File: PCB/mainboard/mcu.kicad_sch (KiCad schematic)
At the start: 10 parts

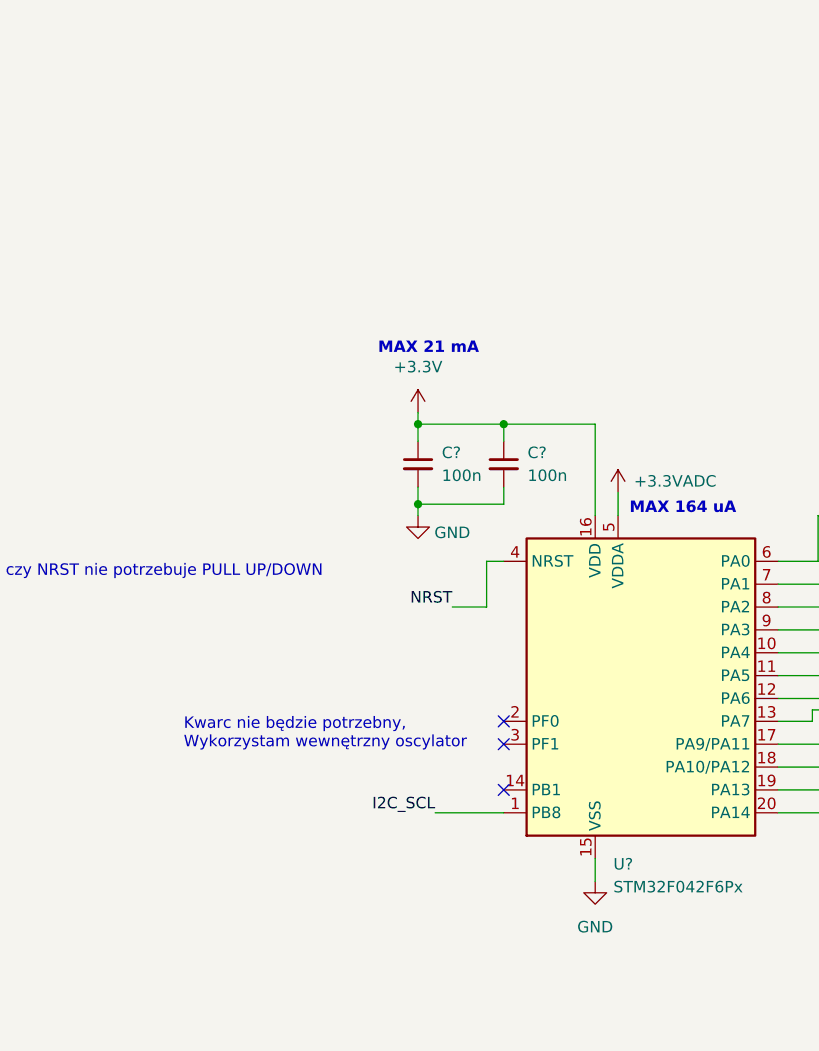
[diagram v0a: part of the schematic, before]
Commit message: Added power up/down push button
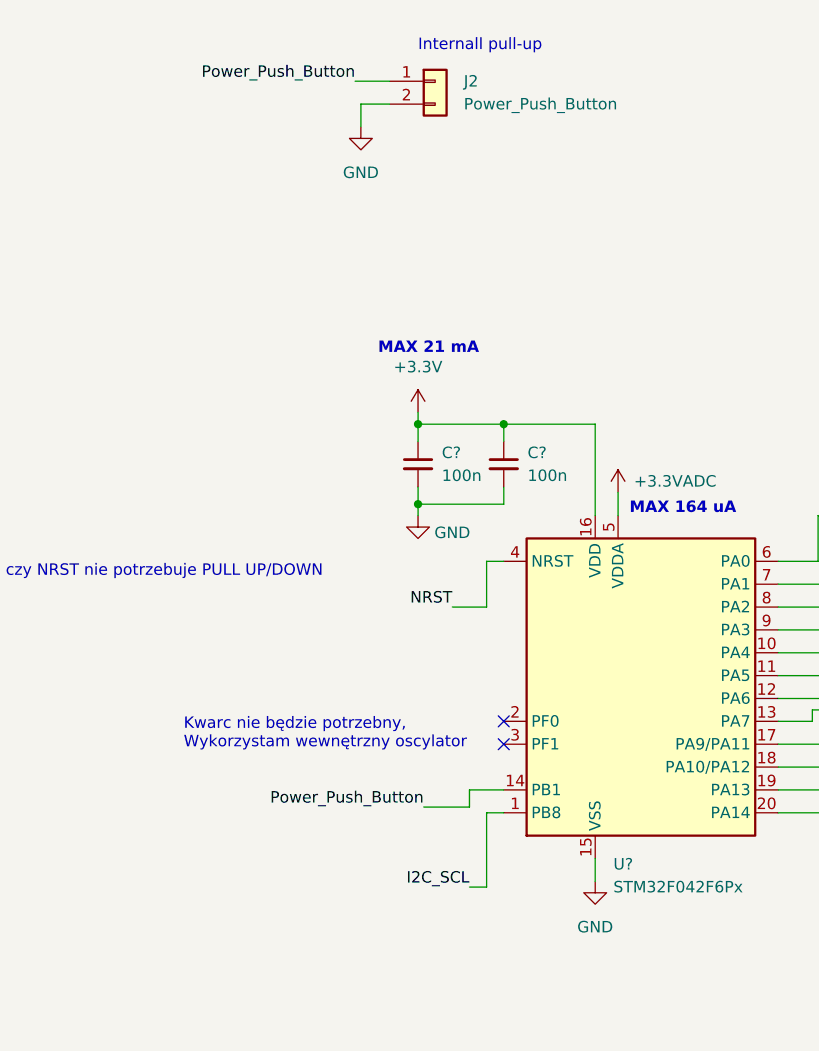
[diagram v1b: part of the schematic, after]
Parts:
- added J2: Power_Push_Button, symbol Connector_Generic:Conn_01x02
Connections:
- net GND: now also J2.2 (Pin_2)
- net Power_Push_Button: now reaches U?.14 (PB1)
- net Power_Push_Button: now also J2.1 (Pin_1)
- no-connect marks 3 -> 2
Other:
- note added: "Internall pull-up"
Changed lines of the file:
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@@
   (junction (at 219.71 131.445) (diameter 0) (color 0 0 0 0)
   )
-  (no_connect (at 120.65 107.95))
   (no_connect (at 120.65 102.87))
   (no_connect (at 120.65 100.33))
@@
     (stroke (width 0) (type default))
   )
-  (wire (pts (xy 113.03 110.49) (xy 120.65 110.49))
+  (wire (pts (xy 116.84 118.745) (xy 118.745 118.745))
     (stroke (width 0) (type default))
   )
@@
     (stroke (width 0) (type default))
   )
+  (wire (pts (xy 104.775 31.75) (xy 107.95 31.75))
+    (stroke (width 0) (type default))
+  )
   (wire (pts (xy 151.13 92.71) (xy 156.21 92.71))
     (stroke (width 0) (type default))
@@
     (stroke (width 0) (type default))
   )
+  (wire (pts (xy 104.775 34.29) (xy 104.775 31.75))
+    (stroke (width 0) (type default))
+  )
   (wire (pts (xy 233.68 58.42) (xy 238.76 58.42))
     (stroke (width 0) (type default))
@@
     (stroke (width 0) (type default))
   )
+  (wire (pts (xy 118.745 118.745) (xy 118.745 110.49))
+    (stroke (width 0) (type default))
+  )
+  (wire (pts (xy 116.84 107.95) (xy 120.65 107.95))
+    (stroke (width 0) (type default))
+  )
   (wire (pts (xy 172.72 34.925) (xy 172.72 34.29))
     (stroke (width 0) (type default))
@@
     (stroke (width 0) (type default))
   )
+  (wire (pts (xy 116.84 109.855) (xy 116.84 107.95))
+    (stroke (width 0) (type default))
+  )
   (wire (pts (xy 233.045 38.1) (xy 238.125 38.1))
     (stroke (width 0) (type default))
@@
     (stroke (width 0) (type default))
   )
+  (wire (pts (xy 104.14 29.21) (xy 107.95 29.21))
+    (stroke (width 0) (type default))
+  )
   (wire (pts (xy 114.935 87.63) (xy 118.745 87.63))
     (stroke (width 0) (type default))
@@
     (stroke (width 0) (type default))
   )
+  (wire (pts (xy 118.745 110.49) (xy 120.65 110.49))
+    (stroke (width 0) (type default))
+  )
   (wire (pts (xy 130.81 77.47) (xy 130.81 67.31))
     (stroke (width 0) (type default))
@@
   )
   (wire (pts (xy 154.94 99.06) (xy 154.94 100.33))
+    (stroke (width 0) (type default))
+  )
+  (wire (pts (xy 111.76 109.855) (xy 116.84 109.855))
     (stroke (width 0) (type default))
   )
@@
     (effects (font (size 1.27 1.27)) (justify left bottom))
   )
+  (text "Internall pull-up" (at 111.125 26.035 0)
+    (effects (font (size 1.27 1.27)) (justify left bottom))
+  )
   (label "Push_Button" (at 156.21 97.79 0) (fields_autoplaced)
     (effects (font (size 1.27 1.27)) (justify left bottom))
@@
     (effects (font (size 1.27 1.27)) (justify right bottom))
   )
-  (label "I2C_SCL" (at 113.03 110.49 180) (fields_autoplaced)
+  (label "Power_Push_Button" (at 111.76 109.855 180) (fields_autoplaced)
+    (effects (font (size 1.27 1.27)) (justify right bottom))
+  )
+  (label "I2C_SCL" (at 116.84 118.745 180) (fields_autoplaced)
     (effects (font (size 1.27 1.27)) (justify right bottom))
   )
@@
   (label "SWDIO" (at 156.21 107.95 0) (fields_autoplaced)
     (effects (font (size 1.27 1.27)) (justify left bottom))
+  )
+  (label "Power_Push_Button" (at 104.14 29.21 180) (fields_autoplaced)
+    (effects (font (size 1.27 1.27)) (justify right bottom))
   )
   (label "SWDIO" (at 233.045 38.1 180) (fields_autoplaced)
@@
     )
   )
+  (symbol (lib_id "Connector_Generic:Conn_01x02") (at 113.03 29.21 0) (unit 1)
+    (in_bom yes) (on_board yes) (dnp no) (fields_autoplaced)
+    (property "Reference" "J2" (at 116.205 29.2099 0)
+      (effects (font (size 1.27 1.27)) (justify left))
+    )
+    (property "Value" "Power_Push_Button" (at 116.205 31.7499 0)
+      (effects (font (size 1.27 1.27)) (justify left))
+    )
+    (property "Footprint" "" (at 113.03 29.21 0)
+      (effects (font (size 1.27 1.27)) hide)
+    )
+    (property "Datasheet" "~" (at 113.03 29.21 0)
+      (effects (font (size 1.27 1.27)) hide)
+    )
+    (pin "1")
+    (pin "2")
+    (instances
+      (project "mainboard"
+        (path "/e63e39d7-6ac0-4ffd-8aa3-1841a4541b55"
+          (reference "J2") (unit 1)
+        )
+        (path "/e63e39d7-6ac0-4ffd-8aa3-1841a4541b55/f2b26c76-d7ac-4ba1-af07-930bed0d7eb8"
+          (reference "J9") (unit 1)
+        )
+      )
+    )
+  )
   (symbol (lib_id "power:GND") (at 234.95 87.63 0) (unit 1)
     (in_bom yes) (on_board yes) (dnp no) (fields_autoplaced)
@@
         )
       )
+    )
+  )
+  (symbol (lib_id "power:GND") (at 104.775 34.29 0) (unit 1)
+    (in_bom yes) (on_board yes) (dnp no) (fields_autoplaced)
+    (property "Reference" "#PWR?" (at 104.775 40.64 0)
+      (effects (font (size 1.27 1.27)) hide)
+    )
+    (property "Value" "GND" (at 104.775 39.37 0)
+      (effects (font (size 1.27 1.27)))
+    )
+    (property "Footprint" "" (at 104.775 34.29 0)
+      (effects (font (size 1.27 1.27)) hide)
+    )
+    (property "Datasheet" "" (at 104.775 34.29 0)
+      (effects (font (size 1.27 1.27)) hide)
+    )
+    (pin "1")
+    (instances
+      (project "mainboard"
+        (path "/e63e39d7-6ac0-4ffd-8aa3-1841a4541b55"
+          (reference "#PWR?") (unit 1)
+        )
+        (path "/e63e39d7-6ac0-4ffd-8aa3-1841a4541b55/f2b26c76-d7ac-4ba1-af07-930bed0d7eb8"
+          (reference "#PWR041") (unit 1)
+        )
+      )
